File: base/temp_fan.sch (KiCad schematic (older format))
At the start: 0 parts

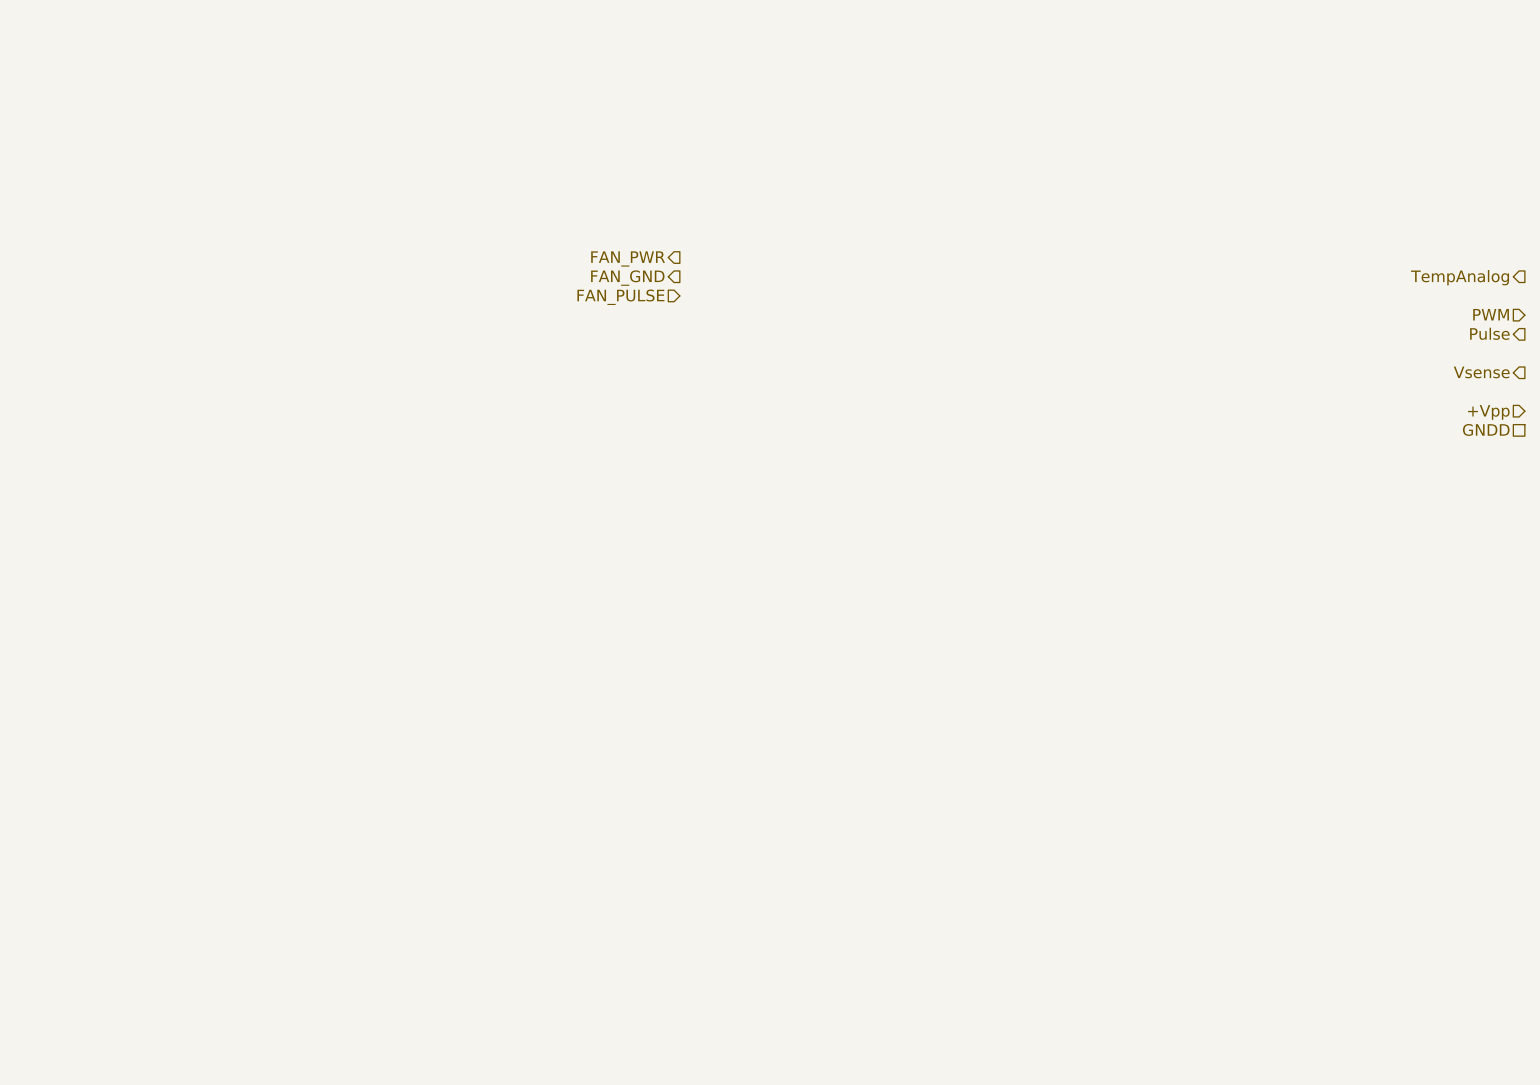
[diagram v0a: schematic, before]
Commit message: temp-sens-fan was created
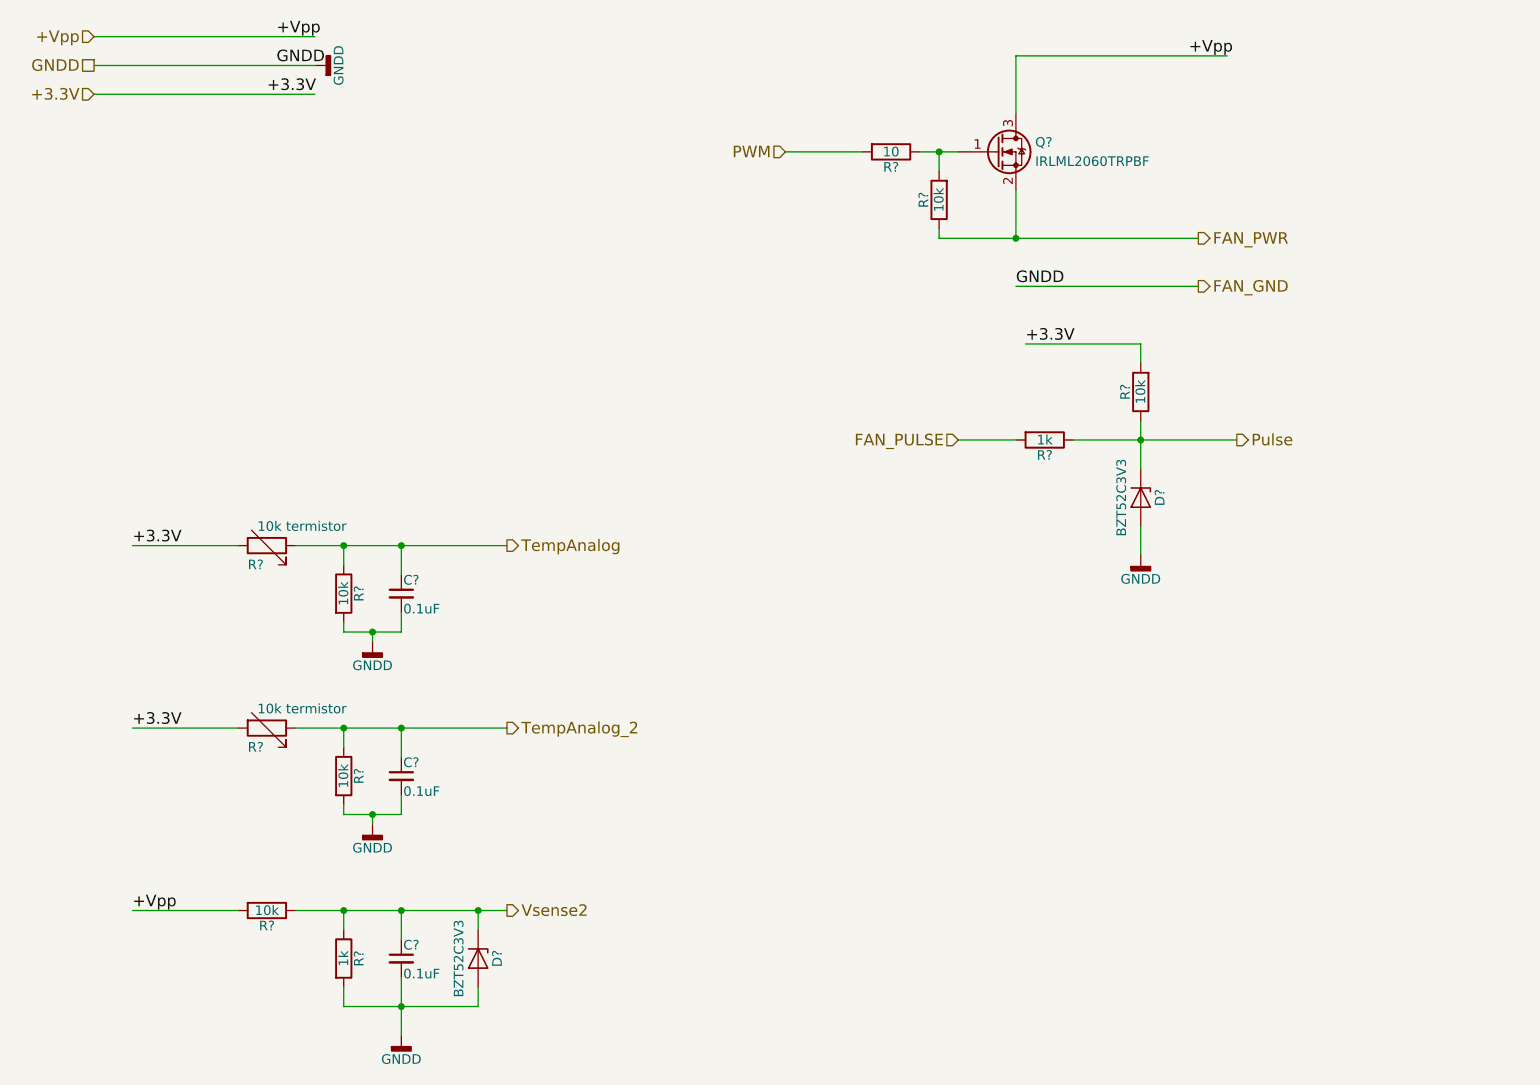
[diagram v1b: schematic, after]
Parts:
- added C? (x3): 0.1uF, Capacitor_SMD:C_0805_2012Metric, symbol C_Small
- added D? (x2): BZT52C3V3, Diode_SMD:D_SOD-123, symbol D_Zener
- added Q?: IRLML2060TRPBF, Package_TO_SOT_SMD:SOT-23, symbol Q_NMOS_GSD
- added R? (x5): 10k, Resistor_SMD:R_0603_1608Metric, symbol R
- added R? (x2): 1k, Resistor_SMD:R_0603_1608Metric, symbol R
- added R?: 10, Resistor_SMD:R_0603_1608Metric, symbol R
- added R? (x2): 10k termistor, Resistor_SMD:R_0805_2012Metric, symbol R_Variable
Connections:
- net labels added: +3.3V, TempAnalog_2, Vsense2
- net labels removed: Vsense
- wire segments 0 -> 43

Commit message: annotate sch
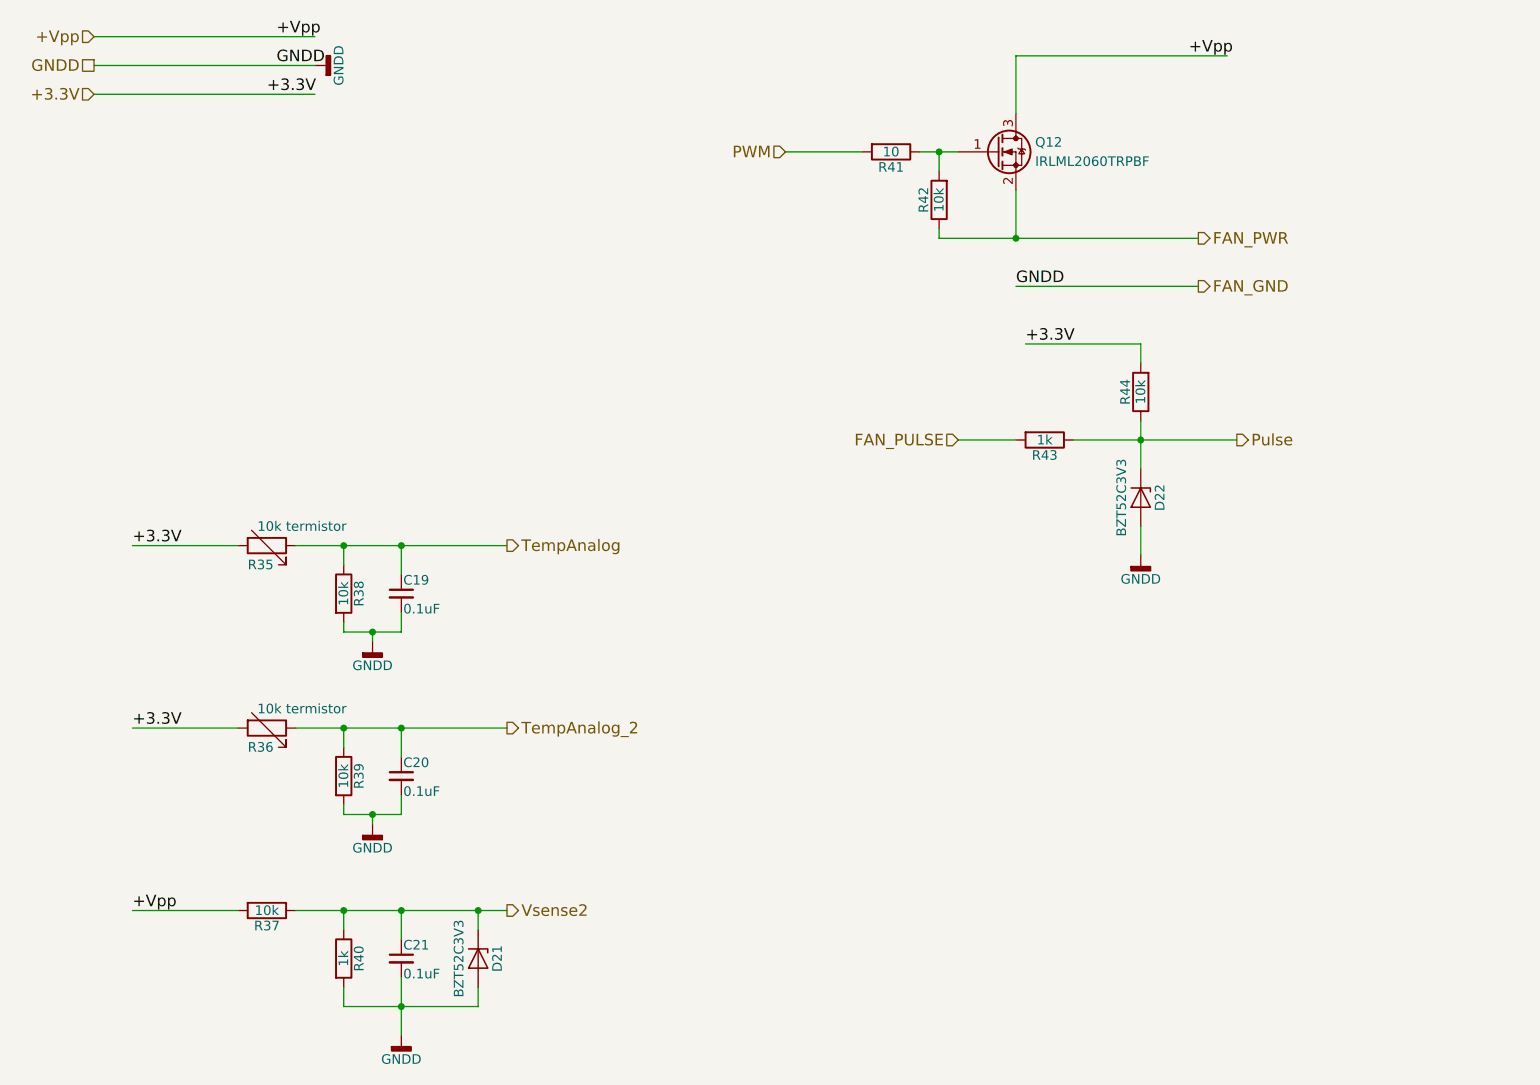
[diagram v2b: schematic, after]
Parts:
- gave numbers to parts that had none: 16
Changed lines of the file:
@@
 TempAnalog_2
 $Comp
-L Q_NMOS_GSD Q?
+L Q_NMOS_GSD Q12
 U 1 1 5A461DD8
 P 5650 1350
-F 0 "Q?" H 5850 1400 50  0000 L CNN
+F 0 "Q12" H 5850 1400 50  0000 L CNN
 F 1 "IRLML2060TRPBF" H 5850 1300 50  0000 L CNN
 F 2 "Package_TO_SOT_SMD:SOT-23" H 5850 1450 50  0001 C CNN
@@
 +3.3V
 $Comp
-L R R?
+L R R38
 U 1 1 5A4729D5
 P 2250 3650
-F 0 "R?" V 2330 3650 50  0000 C CNN
+F 0 "R38" V 2330 3650 50  0000 C CNN
 F 1 "10k" V 2250 3650 50  0000 C CNN
 F 2 "Resistor_SMD:R_0603_1608Metric" V 2180 3650 50  0001 C CNN
@@
 GNDD
 $Comp
-L GNDD #PWR?
+L GNDD #PWR16
 U 1 1 5A472B81
 P 2100 900
-F 0 "#PWR?" H 2100 650 50  0001 C CNN
+F 0 "#PWR16" H 2100 650 50  0001 C CNN
 F 1 "GNDD" H 2100 775 50  0000 C CNN
 F 2 "" H 2100 900 50  0001 C CNN
@@
 $EndComp
 $Comp
-L GNDD #PWR?
+L GNDD #PWR17
 U 1 1 5A472B9C
 P 2400 3900
-F 0 "#PWR?" H 2400 3650 50  0001 C CNN
+F 0 "#PWR17" H 2400 3650 50  0001 C CNN
 F 1 "GNDD" H 2400 3775 50  0000 C CNN
 F 2 "" H 2400 3900 50  0001 C CNN
@@
 +3.3V
 $Comp
-L R R?
+L R R37
 U 1 1 5A475DEB
 P 1850 5300
-F 0 "R?" V 1930 5300 50  0000 C CNN
+F 0 "R37" V 1930 5300 50  0000 C CNN
 F 1 "10k" V 1850 5300 50  0000 C CNN
 F 2 "Resistor_SMD:R_0603_1608Metric" V 1780 5300 50  0001 C CNN
@@
 $EndComp
 $Comp
-L R R?
+L R R40
 U 1 1 5A475DF1
 P 2250 5550
-F 0 "R?" V 2330 5550 50  0000 C CNN
+F 0 "R40" V 2330 5550 50  0000 C CNN
 F 1 "1k" V 2250 5550 50  0000 C CNN
 F 2 "Resistor_SMD:R_0603_1608Metric" V 2180 5550 50  0001 C CNN
@@
 $EndComp
 $Comp
-L GNDD #PWR?
+L GNDD #PWR19
 U 1 1 5A475DF7
 P 2550 5950
-F 0 "#PWR?" H 2550 5700 50  0001 C CNN
+F 0 "#PWR19" H 2550 5700 50  0001 C CNN
 F 1 "GNDD" H 2550 5825 50  0000 C CNN
 F 2 "" H 2550 5950 50  0001 C CNN
@@
 +Vpp
 $Comp
-L R R?
+L R R43
 U 1 1 5A476078
 P 5900 2850
-F 0 "R?" V 5980 2850 50  0000 C CNN
+F 0 "R43" V 5980 2850 50  0000 C CNN
 F 1 "1k" V 5900 2850 50  0000 C CNN
 F 2 "Resistor_SMD:R_0603_1608Metric" V 5830 2850 50  0001 C CNN
@@
 $EndComp
 $Comp
-L R R?
+L R R39
 U 1 1 5A476300
 P 2250 4600
-F 0 "R?" V 2330 4600 50  0000 C CNN
+F 0 "R39" V 2330 4600 50  0000 C CNN
 F 1 "10k" V 2250 4600 50  0000 C CNN
 F 2 "Resistor_SMD:R_0603_1608Metric" V 2180 4600 50  0001 C CNN
@@
 $EndComp
 $Comp
-L GNDD #PWR?
+L GNDD #PWR18
 U 1 1 5A476306
 P 2400 4850
-F 0 "#PWR?" H 2400 4600 50  0001 C CNN
+F 0 "#PWR18" H 2400 4600 50  0001 C CNN
 F 1 "GNDD" H 2400 4725 50  0000 C CNN
 F 2 "" H 2400 4850 50  0001 C CNN
@@
 +3.3V
 $Comp
-L R R?
+L R R41
 U 1 1 5A476F36
 P 5100 1350
-F 0 "R?" V 5180 1350 50  0000 C CNN
+F 0 "R41" V 5180 1350 50  0000 C CNN
 F 1 "10" V 5100 1350 50  0000 C CNN
 F 2 "Resistor_SMD:R_0603_1608Metric" V 5030 1350 50  0001 C CNN
@@
 $EndComp
 $Comp
-L R R?
+L R R42
 U 1 1 5A477022
 P 5350 1600
-F 0 "R?" V 5430 1600 50  0000 C CNN
+F 0 "R42" V 5430 1600 50  0000 C CNN
 F 1 "10k" V 5350 1600 50  0000 C CNN
 F 2 "Resistor_SMD:R_0603_1608Metric" V 5280 1600 50  0001 C CNN
@@
 $EndComp
 $Comp
-L R R?
+L R R44
 U 1 1 5A477E87
 P 6400 2600
-F 0 "R?" V 6480 2600 50  0000 C CNN
+F 0 "R44" V 6480 2600 50  0000 C CNN
 F 1 "10k" V 6400 2600 50  0000 C CNN
 F 2 "Resistor_SMD:R_0603_1608Metric" V 6330 2600 50  0001 C CNN
@@
 +3.3V
 $Comp
-L D_Zener D?
+L D_Zener D22
 U 1 1 5A4780DE
 P 6400 3150
-F 0 "D?" H 6400 3250 50  0000 C CNN
+F 0 "D22" H 6400 3250 50  0000 C CNN
 F 1 "BZT52C3V3" H 6400 3050 50  0000 C CNN
 F 2 "Diode_SMD:D_SOD-123" H 6400 3150 50  0001 C CNN
@@
 Connection ~ 6400 2850
 $Comp
-L GNDD #PWR?
+L GNDD #PWR20
 U 1 1 5A4783AF
 P 6400 3450
-F 0 "#PWR?" H 6400 3200 50  0001 C CNN
+F 0 "#PWR20" H 6400 3200 50  0001 C CNN
 F 1 "GNDD" H 6400 3325 50  0000 C CNN
 F 2 "" H 6400 3450 50  0001 C CNN
@@
 	1700 4350 1150 4350
 $Comp
-L R_Variable R?
+L R_Variable R35
 U 1 1 5A47A00D
 P 1850 3400
-F 0 "R?" V 1950 3300 50  0000 L CNN
+F 0 "R35" V 1950 3300 50  0000 L CNN
 F 1 "10k termistor" V 1750 3350 50  0000 L CNN
 F 2 "Resistor_SMD:R_0805_2012Metric" V 1780 3400 50  0001 C CNN
@@
 $EndComp
 $Comp
-L R_Variable R?
+L R_Variable R36
 U 1 1 5A47A0FF
 P 1850 4350
-F 0 "R?" V 1950 4250 50  0000 L CNN
+F 0 "R36" V 1950 4250 50  0000 L CNN
 F 1 "10k termistor" V 1750 4300 50  0000 L CNN
 F 2 "Resistor_SMD:R_0805_2012Metric" V 1780 4350 50  0001 C CNN
@@
 	1700 5300 1150 5300
 $Comp
-L C_Small C?
+L C_Small C19
 U 1 1 5A47A7FA
 P 2550 3650
-F 0 "C?" H 2560 3720 50  0000 L CNN
+F 0 "C19" H 2560 3720 50  0000 L CNN
 F 1 "0.1uF" H 2560 3570 50  0000 L CNN
 F 2 "Capacitor_SMD:C_0805_2012Metric" H 2550 3650 50  0001 C CNN
@@
 	2250 3850 2550 3850
 $Comp
-L C_Small C?
+L C_Small C20
 U 1 1 5A47A90E
 P 2550 4600
-F 0 "C?" H 2560 4670 50  0000 L CNN
+F 0 "C20" H 2560 4670 50  0000 L CNN
 F 1 "0.1uF" H 2560 4520 50  0000 L CNN
 F 2 "Capacitor_SMD:C_0805_2012Metric" H 2550 4600 50  0001 C CNN
@@
 Connection ~ 2400 4800
 $Comp
-L D_Zener D?
+L D_Zener D21
 U 1 1 5A47B4B9
 P 2950 5550
-F 0 "D?" H 2950 5650 50  0000 C CNN
+F 0 "D21" H 2950 5650 50  0000 C CNN
 F 1 "BZT52C3V3" H 2950 5450 50  0000 C CNN
 F 2 "Diode_SMD:D_SOD-123" H 2950 5550 50  0001 C CNN
@@
 	2250 5800 2950 5800
 $Comp
-L C_Small C?
+L C_Small C21
 U 1 1 5A47D661
 P 2550 5550
-F 0 "C?" H 2560 5620 50  0000 L CNN
+F 0 "C21" H 2560 5620 50  0000 L CNN
 F 1 "0.1uF" H 2560 5470 50  0000 L CNN
 F 2 "Capacitor_SMD:C_0805_2012Metric" H 2550 5550 50  0001 C CNN

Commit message: upd
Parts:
- renumbered C19 to C17, C20 to C18, C21 to C19
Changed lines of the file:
@@
 	1700 5300 1150 5300
 $Comp
-L C_Small C19
+L C_Small C17
 U 1 1 5A47A7FA
 P 2550 3650
-F 0 "C19" H 2560 3720 50  0000 L CNN
+F 0 "C17" H 2560 3720 50  0000 L CNN
 F 1 "0.1uF" H 2560 3570 50  0000 L CNN
 F 2 "Capacitor_SMD:C_0805_2012Metric" H 2550 3650 50  0001 C CNN
@@
 	2250 3850 2550 3850
 $Comp
-L C_Small C20
+L C_Small C18
 U 1 1 5A47A90E
 P 2550 4600
-F 0 "C20" H 2560 4670 50  0000 L CNN
+F 0 "C18" H 2560 4670 50  0000 L CNN
 F 1 "0.1uF" H 2560 4520 50  0000 L CNN
 F 2 "Capacitor_SMD:C_0805_2012Metric" H 2550 4600 50  0001 C CNN
@@
 	2250 5800 2950 5800
 $Comp
-L C_Small C21
+L C_Small C19
 U 1 1 5A47D661
 P 2550 5550
-F 0 "C21" H 2560 5620 50  0000 L CNN
+F 0 "C19" H 2560 5620 50  0000 L CNN
 F 1 "0.1uF" H 2560 5470 50  0000 L CNN
 F 2 "Capacitor_SMD:C_0805_2012Metric" H 2550 5550 50  0001 C CNN
